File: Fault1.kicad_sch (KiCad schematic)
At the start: 26 parts

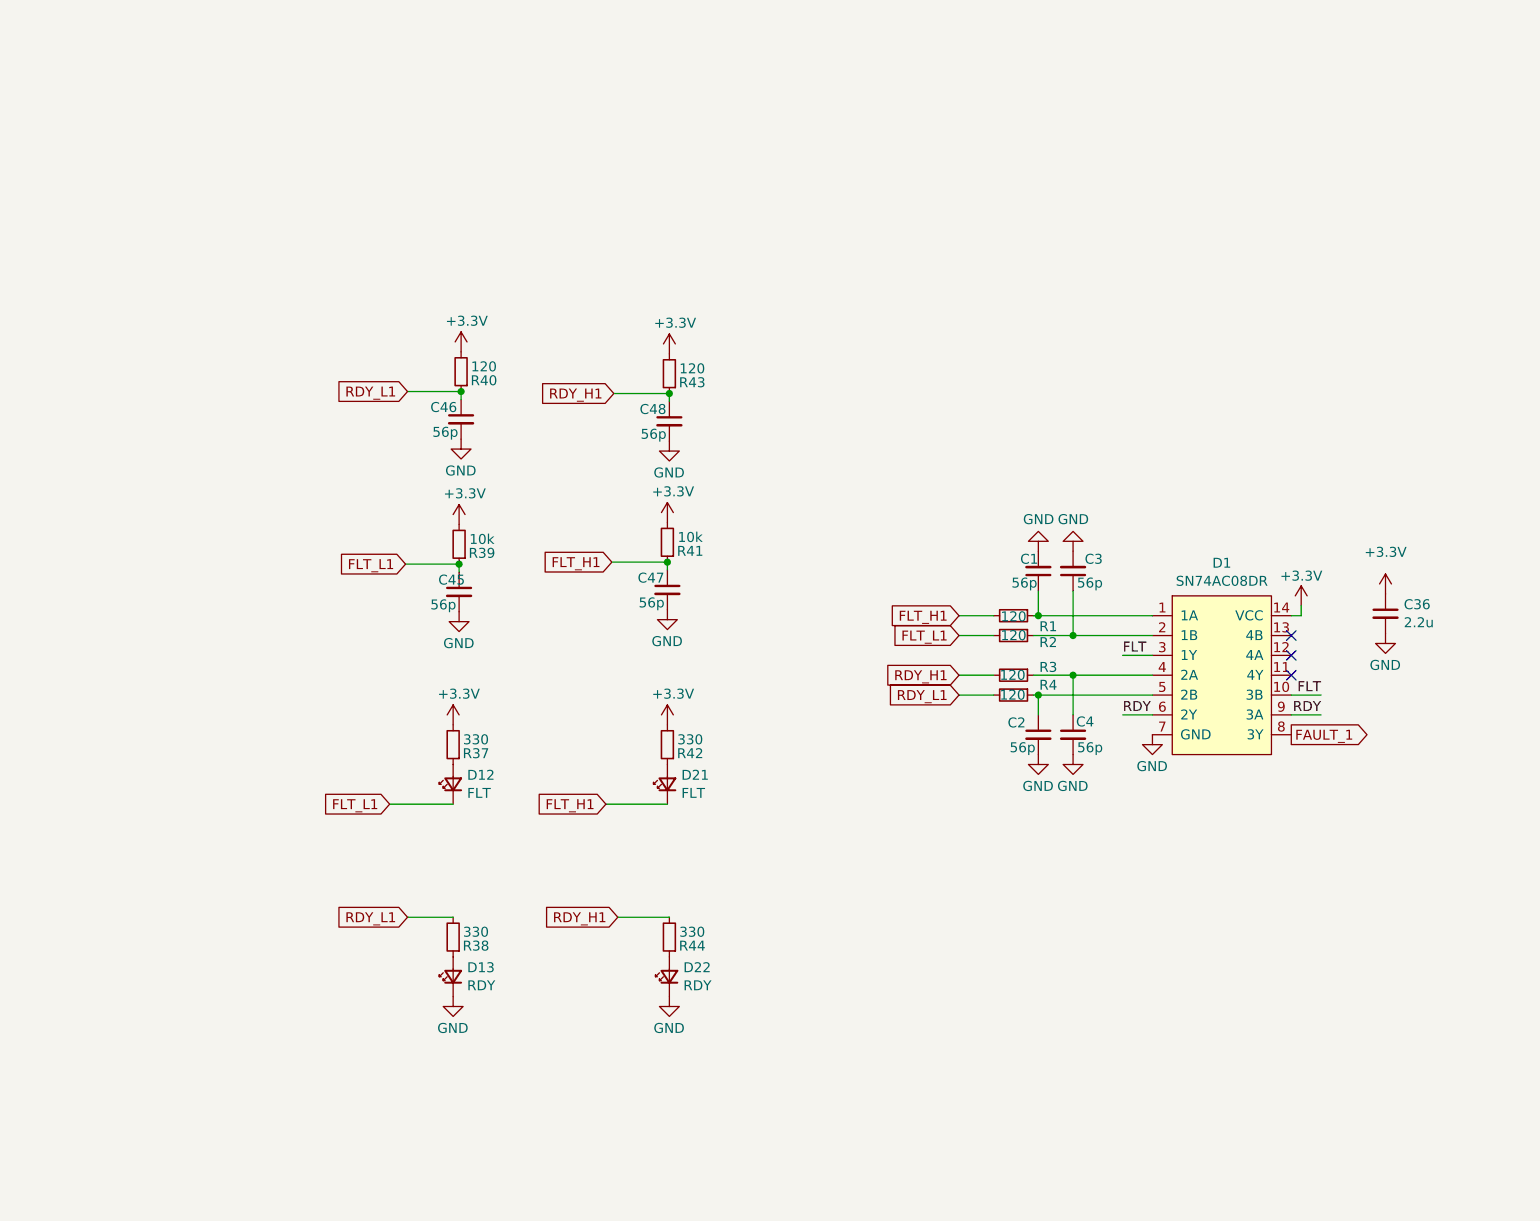
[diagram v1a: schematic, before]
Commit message: Изменил схему
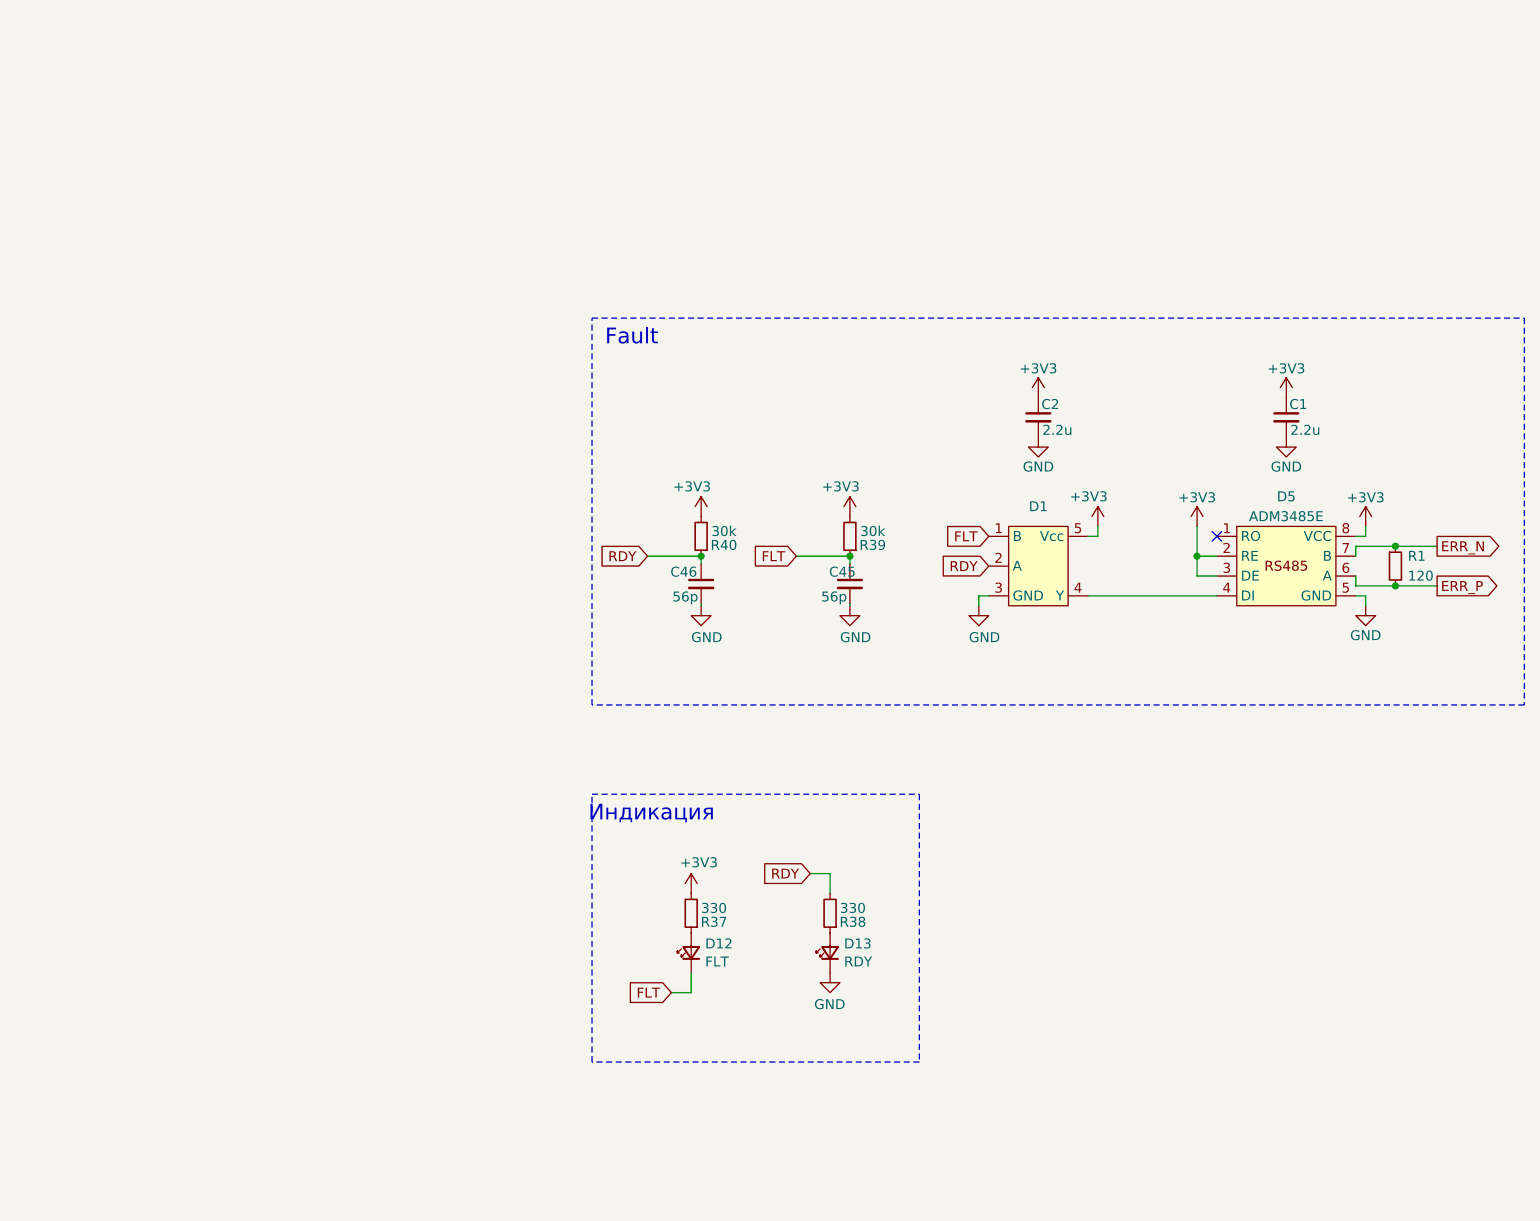
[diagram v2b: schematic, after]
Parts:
- removed C3, C4, C47, C48: 56p, Capacitor_SMD:C_0805_2012Metric_Pad1.18x1.45mm_HandSolder, symbol Device:C_Small
- removed C36: 2.2u, Capacitor_SMD:C_0805_2012Metric_Pad1.18x1.45mm_HandSolder, symbol Device:C_Small
- removed D1: SN74AC08DR, Package_SO:SOIC-14_3.9x8.7mm_P1.27mm, symbol Logic:SN74AC08DR
- removed D21: FLT, LED_SMD:LED_0805_2012Metric_Pad1.15x1.40mm_HandSolder, symbol Device:LED_Small
- removed D22: RDY, LED_SMD:LED_0805_2012Metric_Pad1.15x1.40mm_HandSolder, symbol Device:LED_Small
- removed R2, R3, R4, R43: 120, Resistor_SMD:R_0805_2012Metric_Pad1.20x1.40mm_HandSolder, symbol Device:R_Small
- removed R41: 10k, Resistor_SMD:R_0805_2012Metric_Pad1.20x1.40mm_HandSolder, symbol Device:R_Small
- removed R42, R44: 330, Resistor_SMD:R_0805_2012Metric_Pad1.20x1.40mm_HandSolder, symbol Device:R_Small
- added D1: ~, symbol Logic_My:MC74VHC1GT08DTT1G
- added D5: ADM3485E, Package_SO:SOIC-8_3.9x4.9mm_P1.27mm, symbol Interface_My:ADM3485E_1
- C1, C2: value 56p -> 2.2u
- R39: value 10k -> 30k
- R40: value 120 -> 30k
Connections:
- net FLT_L1 is gone; now on net FLT: C45.1, D12.1 (K), R39.1
- net RDY_L1 is gone; now on net RDY: C46.1, R38.2, R40.1
- net +3V3: now also C1.1, C2.1, D1.5 (Vcc), D5.2 (RE), D5.3 (DE), D5.8 (VCC)
- net FLT: now also D1.1 (B)
- net GND: now also D1.3 (GND), D5.5 (GND)
- net RDY: now also D1.2 (A)
- net ERR_N: now reaches R1.1
- net ERR_N: now also D5.7 (B); no longer C1.1
- net FLT_H1 renamed ERR_P
- net ERR_P: now also D5.6 (A)
- new net: D1.4 (Y), D5.4 (DI)
- no-connect marks 3 -> 1
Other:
- note added: "Fault"
- note added: "Индикация"
- moved on the sheet: C45, C46, D12, D13, R37, R38, R39, R40

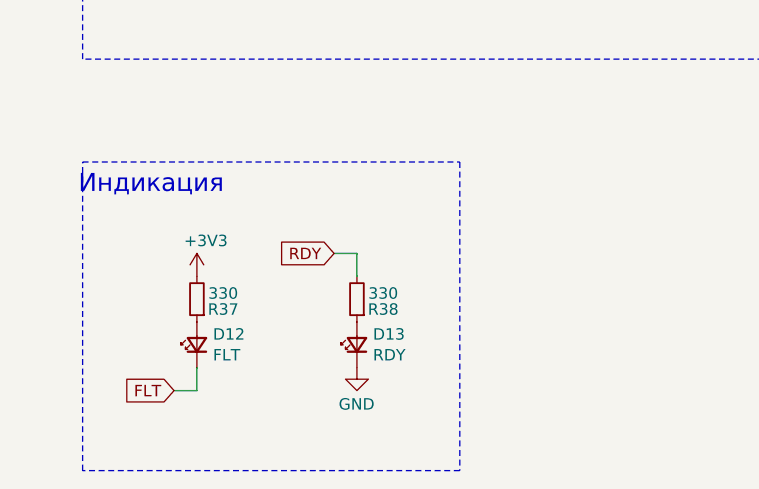
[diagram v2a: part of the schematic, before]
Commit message: Разместил все три стойки в своей области
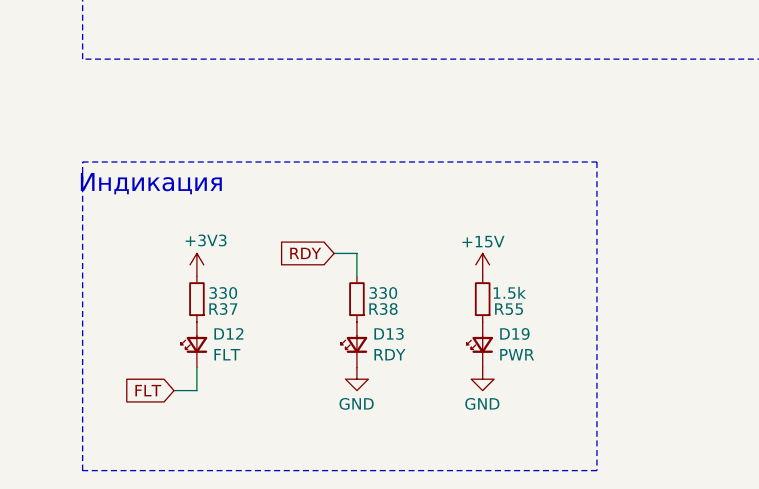
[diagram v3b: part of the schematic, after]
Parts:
- added D19: PWR, LED_SMD:LED_0805_2012Metric_Pad1.15x1.40mm_HandSolder, symbol Device:LED_Small
- added R55: 1.5k, Resistor_SMD:R_0805_2012Metric_Pad1.20x1.40mm_HandSolder, symbol Device:R_Small
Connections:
- net GND: now also D19.1 (K)
- new net: D19.2 (A), R55.1
- new net +15V: R55.2
